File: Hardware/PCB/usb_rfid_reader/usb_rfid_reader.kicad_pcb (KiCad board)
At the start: 2 copper layers, 75 x 75 mm, 35 parts, among them J1 Conn_01x08, J2 Conn_ST_STDC14, J3 10172013-00011LF, Q1 2N3904, SW1 RESET, U1 STM32L476RGTx, U2 AZ1117CH2-3.3, U3 USBLC6-2P6

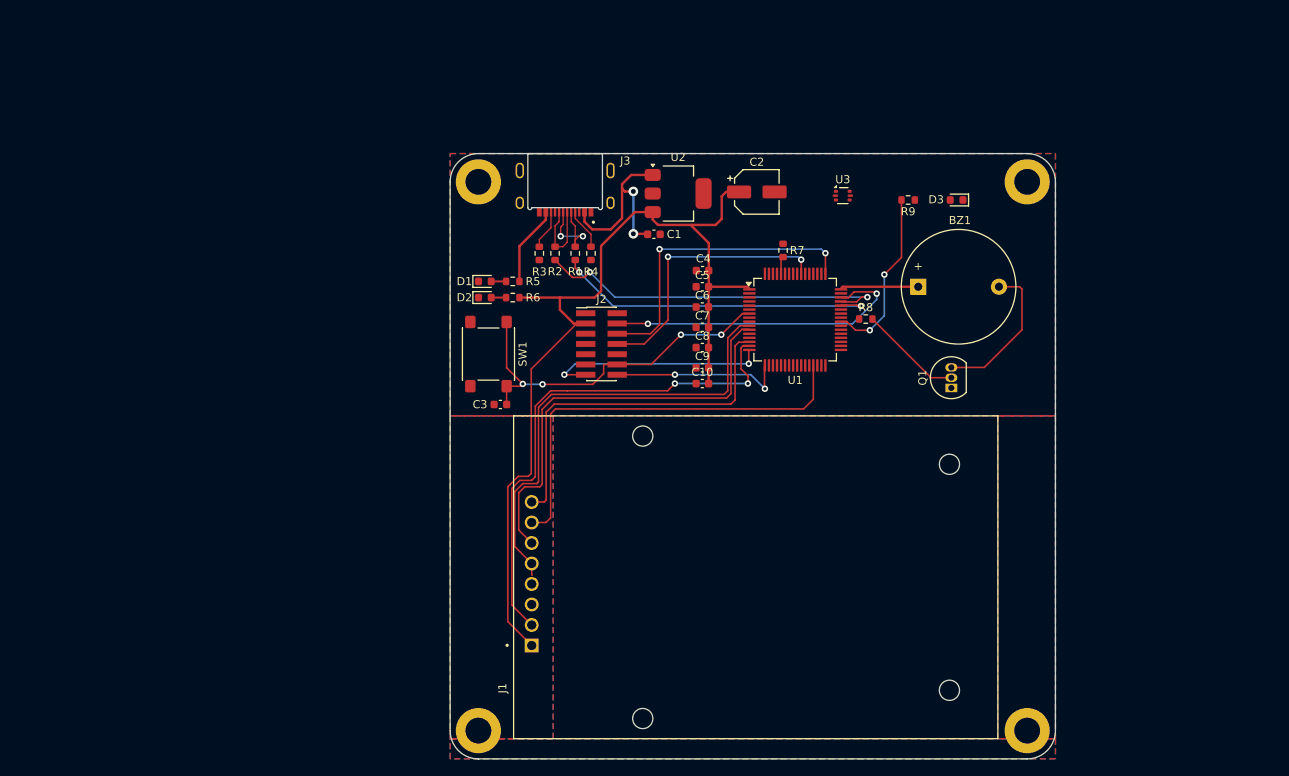
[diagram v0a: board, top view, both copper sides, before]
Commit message: Initialisation du projet Django
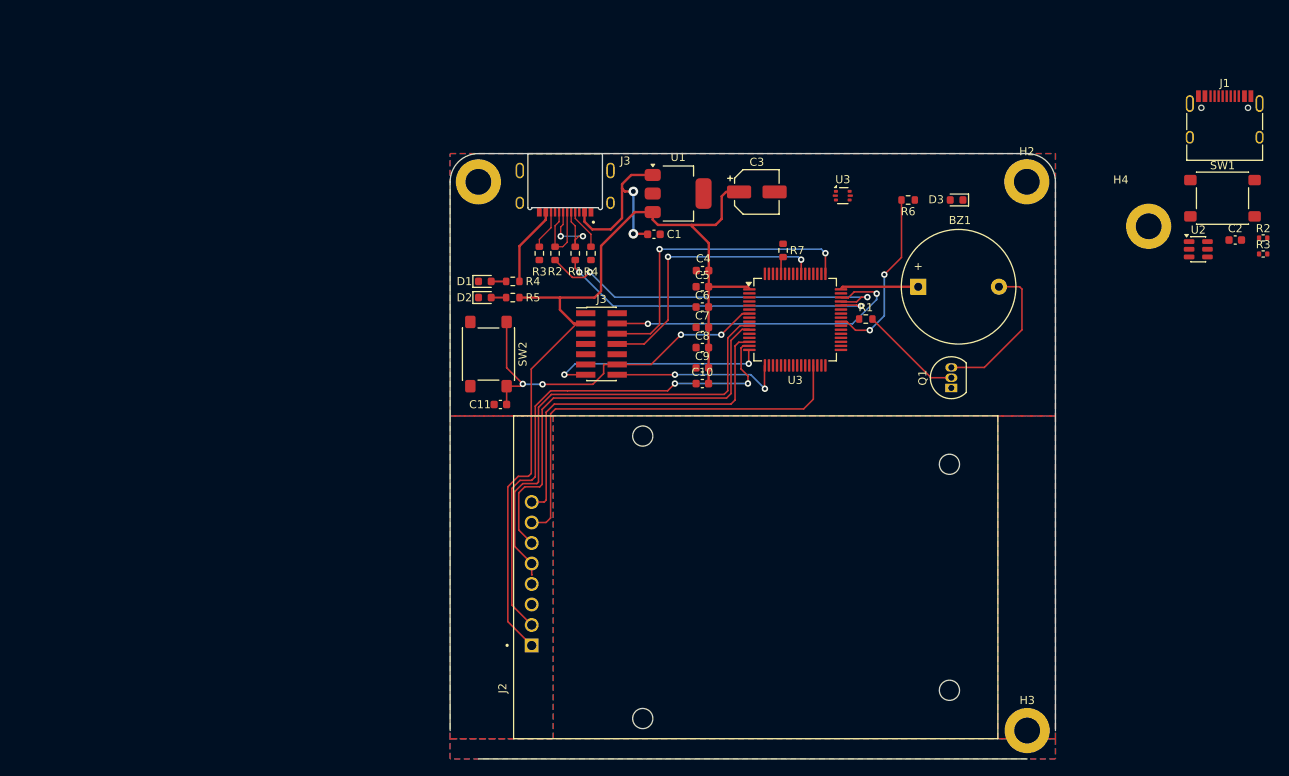
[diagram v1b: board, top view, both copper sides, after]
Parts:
- removed H1: MountingHole_Pad, MountingHole:MountingHole_3.2mm_M3_DIN965_Pad
- added C2: 1u, Capacitor_SMD:C_0603_1608Metric, F.Cu at (206.0, 70.7)
- added H3: MountingHole_Pad, MountingHole:MountingHole_3.2mm_M3_DIN965_Pad, F.Cu at (180.2, 131.4)
- added J1: 629722000214, Connector_USB:USB_C_Receptacle_HRO_TYPE-C-31-M-12, F.Cu at (204.7, 56.9)
- added R2: 5k1, Resistor_SMD:R_0402_1005Metric, F.Cu at (209.5, 70.4)
- added R3: 5k1, Resistor_SMD:R_0402_1005Metric, F.Cu at (209.5, 72.4)
- added SW1: RESET, Button_Switch_SMD:SW_SPST_PTS645Sx43SMTR92, F.Cu at (204.4, 65.5)
- added U2: USBLC6-2SC6, Package_TO_SOT_SMD:SOT-23-6, F.Cu at (201.4, 71.8)
- C10: value 100n -> 10n
- R4: renamed from R5; value 3k -> 680R
- R5: renamed from R6; value 1.5k -> 300R
- R6: renamed from R9; value 1.5k -> 300R
- moved H2 96.1 mm to (180.2, 63.5)
- moved H4 16.0 mm to (195.3, 69.0)
- renumbered C3 to C11, C2 to C3, J1 to J2, J2 to J3, R8 to R1, SW1 to SW2, U2 to U1, U1 to U3
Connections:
- net BUZZ renamed /BUZZ_TIM1
- net NRST renamed /NRST
- net Net-(U1-BOOT0) renamed /BOOT0
- net SWCLK renamed /SWCLK
- net SWDIO renamed /SWDIO
- net SWO renamed /SWO
- net USER_LED renamed /USER_LED
- J2 pad 2: SPI2_RST -> /RC522_RST
- J2 pad 5: SPI2_MISO -> /RC522_SPI2_MISO
- J2 pad 6: SPI2_MOSI -> /RC522_SPI2_MOSI
- J2 pad 7: SPI2_SCK -> /RC522_SPI2_CLK
- J2 pad 8: SPI2_SDA -> /RC522_SPI2_CE_N
- J3 pad 13: USART2_TX -> /VCP_USART2_RX
- J3 pad 14: USART2_RX -> /VCP_USART2_TX
- U3 pad 10: SPI2_MISO -> unconnected-(U3-PC2-Pad10)
- U3 pad 11: SPI2_MOSI -> unconnected-(U3-PC3-Pad11)
- U3 pad 14: SPI2_SDA -> unconnected-(U3-PA0-Pad14)
- U3 pad 15: SPI2_RST -> unconnected-(U3-PA1-Pad15)
- U3 pad 16: USART2_TX -> /VCP_USART2_TX
- U3 pad 17: USART2_RX -> /VCP_USART2_RX
- U3 pad 29: SPI2_SCK -> unconnected-(U3-PB10-Pad29)
- U3 pad 33: unconnected-(U1-PB12-Pad33) -> /RC522_SPI2_CE_N
- U3 pad 34: unconnected-(U1-PB13-Pad34) -> /RC522_SPI2_CLK
- U3 pad 35: unconnected-(U1-PB14-Pad35) -> /RC522_SPI2_MISO
- U3 pad 36: unconnected-(U1-PB15-Pad36) -> /RC522_SPI2_MOSI
- U3 pad 37: unconnected-(U1-PC6-Pad37) -> /RC522_RST
- U3 pad 44: USB_DM -> /USB_DM
- U3 pad 45: USB_DP -> /USB_DP
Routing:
- net (no net): track 0.00 -> 323.0 mm, vias 0 -> 6
- net SPI2_RST: track 63.6 -> 0.00 mm, vias 2 -> 0
- net SPI2_MISO: track 58.1 -> 0.00 mm
- net SPI2_MOSI: track 53.2 -> 0.00 mm
- net SPI2_SCK: track 53.0 -> 0.00 mm
- net SPI2_SDA: track 45.5 -> 0.00 mm
- net USART2_TX: track 27.8 -> 0.00 mm, vias 2 -> 0
- net USART2_RX: track 21.9 -> 0.00 mm, vias 2 -> 0

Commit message: modification classes jango
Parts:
- added H1: MountingHole_Pad, MountingHole:MountingHole_3.2mm_M3_DIN965_Pad, F.Cu at (197.9, 97.5)
- J1: footprint Connector_USB:USB_C_Receptacle_HRO_TYPE-C-31-M-12 -> 10172013-00011LF:AMPHENOL_10172013-00011LF
- moved J1 80.7 mm to (124.1, 53.1)

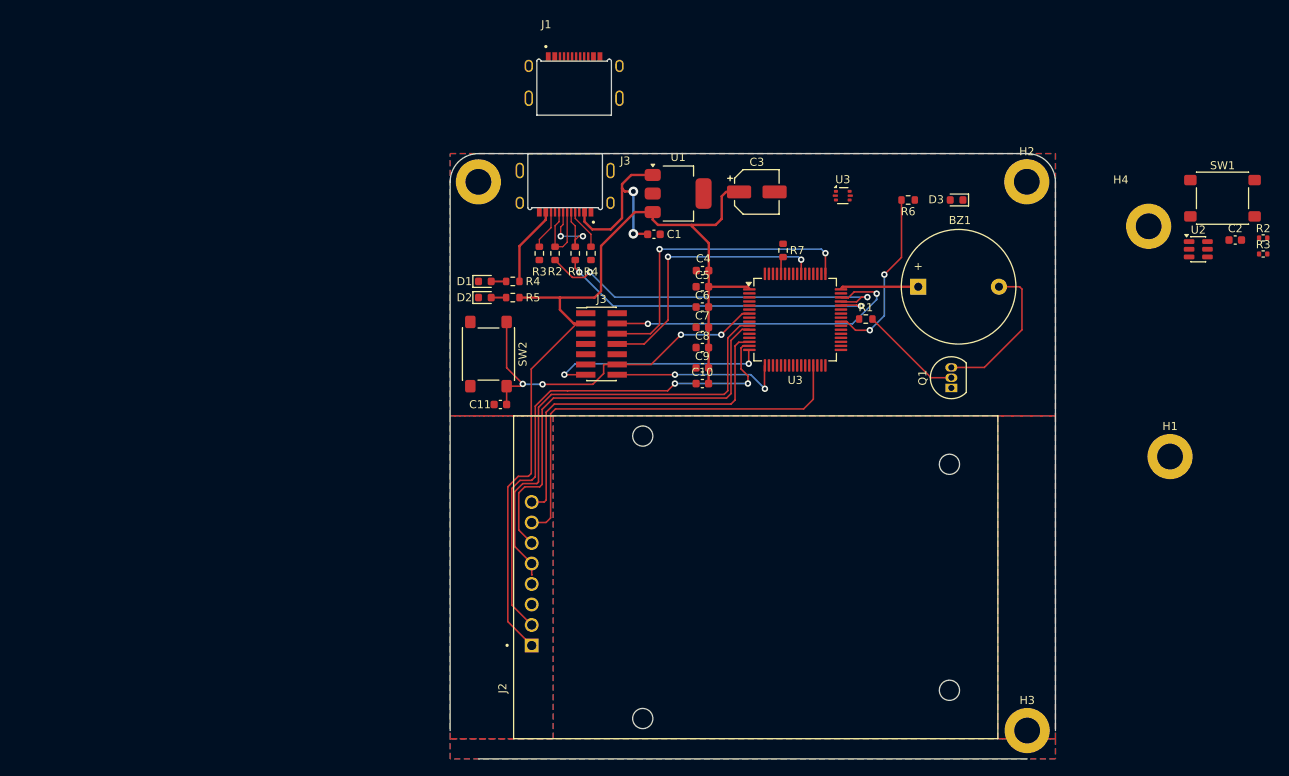
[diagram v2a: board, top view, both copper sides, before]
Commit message: routage PCB avant ERC
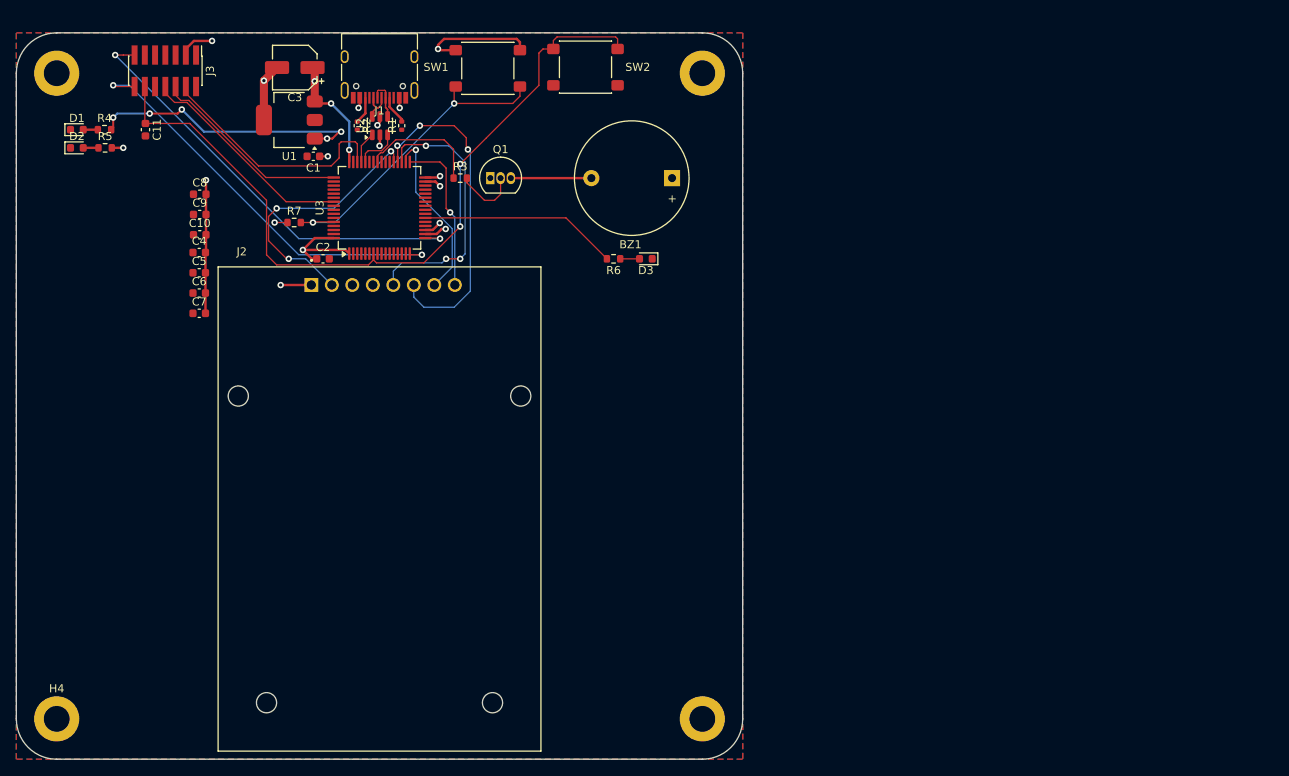
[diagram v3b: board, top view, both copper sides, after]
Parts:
- removed the H3 at (112.2, 63.5)
- removed the H3 at (180.2, 131.4)
- removed the J3 at (123.0, 62.1)
- removed the J3 at (127.5, 83.5)
- removed the R1 at (160.2, 80.5)
- removed the R1 at (124.2, 72.3)
- removed the R2 at (209.5, 70.4)
- removed the R2 at (121.8, 72.3)
- removed the R3 at (209.5, 72.4)
- removed the R3 at (119.8, 72.3)
- removed the R4 at (116.5, 75.8)
- removed the R4 at (126.2, 72.3)
- removed the U3 at (157.4, 65.2)
- removed the U3 at (151.5, 80.5)
- added H3: MountingHole_Pad, MountingHole:MountingHole_3.2mm_M3_DIN965_Pad, F.Cu at (140.0, 130.0)
- added J3: Conn_ST_STDC14, Connector_PinHeader_1.27mm:PinHeader_2x07_P1.27mm_Vertical_SMD, F.Cu at (73.5, 49.7)
- added R1: 5k1, Resistor_SMD:R_0402_1005Metric, F.Cu at (102.8, 56.5)
- added R2: 5k1, Resistor_SMD:R_0402_1005Metric, F.Cu at (97.2, 56.5)
- added R3: 1k, Resistor_SMD:R_0603_1608Metric, F.Cu at (110.0, 63.0)
- added R4: 680R, Resistor_SMD:R_0603_1608Metric, F.Cu at (65.9, 57.0)
- added U3: STM32L476RGTx, Package_QFP:LQFP-64_10x10mm_P0.5mm, F.Cu at (100.0, 66.7)
- J1: footprint 10172013-00011LF:AMPHENOL_10172013-00011LF -> Connector_USB:USB_C_Receptacle_HRO_TYPE-C-31-M-12
- moved H4 148.4 mm to (60.0, 130.0)
- moved H1 145.9 mm to (60.0, 50.0)
- moved C2 113.1 mm to (93.0, 73.0)
- moved U2 102.6 mm to (100.0, 56.5), turned to 90 degrees
- moved SW1 92.4 mm to (113.4, 49.4)
- moved C8 65.1 mm to (77.7, 65.0)
- moved C9 65.1 mm to (77.7, 67.5)
- moved C10 64.9 mm to (77.7, 70.0)
- moved Q1 62.8 mm to (113.7, 63.0), turned to 0 degrees
- moved C4 62.4 mm to (77.7, 72.2)
- moved C5 62.4 mm to (77.7, 74.7)
- moved C6 62.4 mm to (77.7, 77.2)
- moved C7 62.4 mm to (77.7, 79.8)
- moved R7 60.7 mm to (89.4, 68.5), turned to 0 degrees
- moved C3 59.3 mm to (89.5, 49.3), turned to 180 degrees
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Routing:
- net (no net): track 323.0 -> 0.00 mm, vias 6 -> 0
- net +3.3V: track 126.7 -> 72.3 mm, vias 0 -> 11
- net /VCP_USART2_RX: track 0.00 -> 53.9 mm, vias 0 -> 2
- net /VCP_USART2_TX: track 0.00 -> 51.2 mm, vias 0 -> 2
- net /NRST: track 45.3 -> 96.0 mm, vias 4 -> 2
- net USB_DP: track 44.7 -> 0.00 mm, vias 2 -> 0
- net /RC522_SPI2_MOSI: track 0.00 -> 41.3 mm, vias 0 -> 3
- net USB_DM: track 40.9 -> 0.00 mm, vias 2 -> 0
- net /BOOT0: track 2.18 -> 39.6 mm, vias 0 -> 2
- net /RC522_SPI2_MISO: track 0.00 -> 33.5 mm, vias 0 -> 3
- net /RC522_RST: track 0.00 -> 33.1 mm, vias 0 -> 3
- net /RC522_SPI2_CLK: track 0.00 -> 21.8 mm, vias 0 -> 1
- net /RC522_SPI2_CE_N: track 0.00 -> 19.7 mm, vias 0 -> 1
- net /BUZZ_TIM1: track 0.00 -> 15.1 mm
- net GND: track 0.00 -> 15.0 mm, vias 0 -> 5
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- added copper zone on In1.Cu, net +3.3V
- added copper zone on In1.Cu, net +5V
- added copper zone on In2.Cu, net GND
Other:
- board size 75 x 75 mm -> 90 x 90 mm
- copper layers 2 -> 4

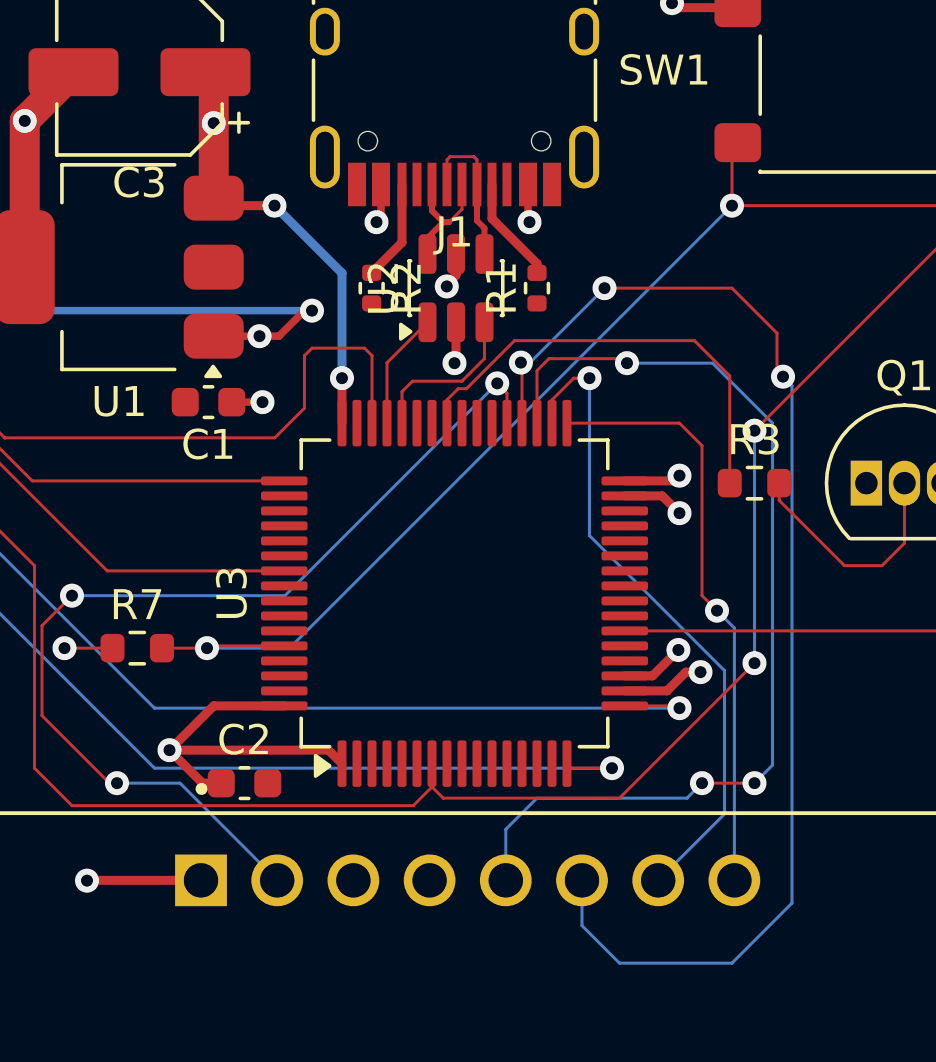
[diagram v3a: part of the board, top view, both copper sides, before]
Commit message: correctif erreur routage
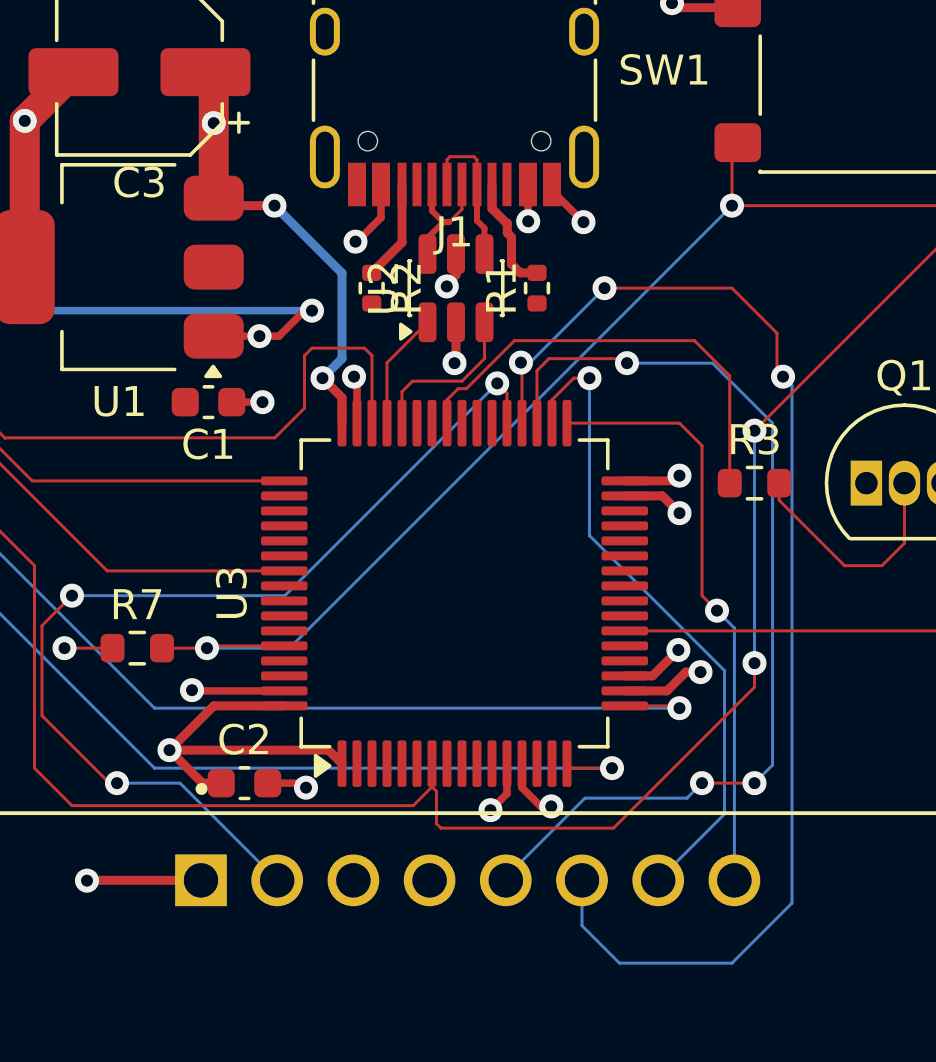
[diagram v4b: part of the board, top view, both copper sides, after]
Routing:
- net GND: track 15.0 -> 24.5 mm, vias 5 -> 10
- net +3.3V: track 72.3 -> 74.8 mm, vias 11 -> 12
- net /NRST: track 96.0 -> 97.9 mm
- net /RC522_SPI2_MISO: track 33.5 -> 32.6 mm
- net +5V: track 39.9 -> 40.8 mm
